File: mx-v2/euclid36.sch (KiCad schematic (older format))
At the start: 114 parts, among them SW1 RotaryEncoder_Switch, SW10 SW_PUSH, SW11 SW_PUSH, SW12 SW_PUSH, SW14 SW_PUSH, SW15 SW_PUSH, SW16 SW_PUSH, SW17 SW_PUSH, SW18 SW_PUSH, SW19 SW_PUSH, SW2 SW_PUSH, SW20 SW_PUSH, SW21 SW_PUSH, SW22 SW_PUSH, SW23 SW_PUSH, SW25 SW_PUSH, SW26 SW_PUSH, SW27 SW_PUSH, SW28 SW_PUSH, SW29 SW_PUSH, SW3 SW_PUSH, SW31 SW_PUSH, SW32 SW_PUSH, SW33 SW_PUSH, SW34 SW_PUSH, SW35 SW_PUSH, SW37 SW_PUSH, SW38 SW_PUSH, SW39 SW_PUSH, SW4 SW_PUSH, SW40 SW_PUSH, SW41 SW_PUSH, SW42 SW_PUSH, SW5 SW_PUSH, SW6 SW_PUSH, SW7 RotaryEncoder_Switch, SW8 SW_PUSH, SW9 SW_PUSH, U1 USBLC6-2SC6, U2 ATmega32U4-AU, Y1 XTAL

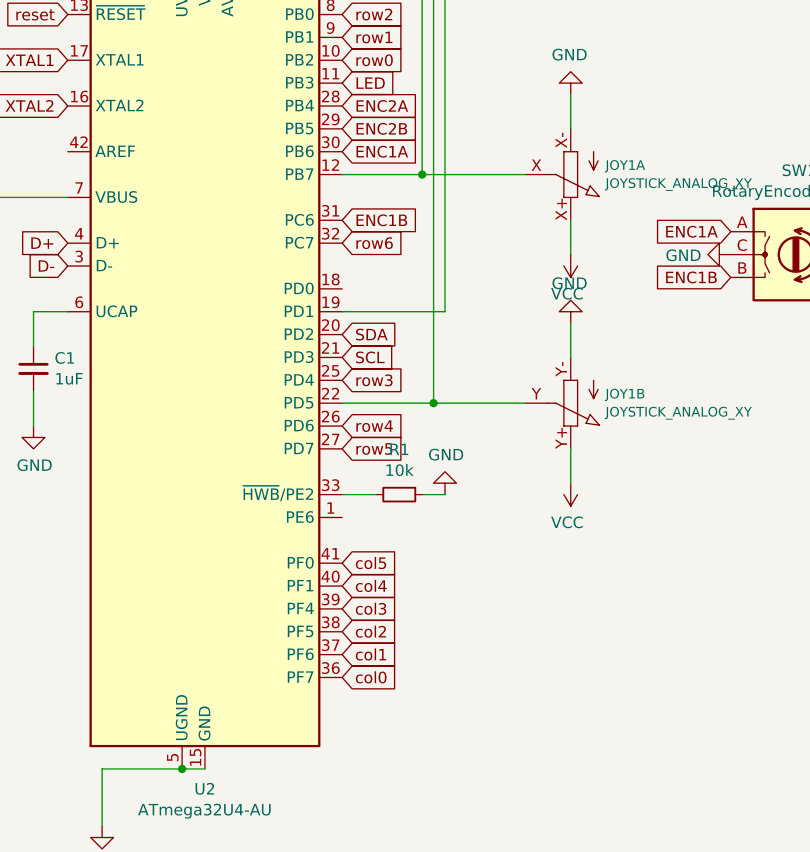
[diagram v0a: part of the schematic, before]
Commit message: accidentally wired my analog joysticks to digital inputs
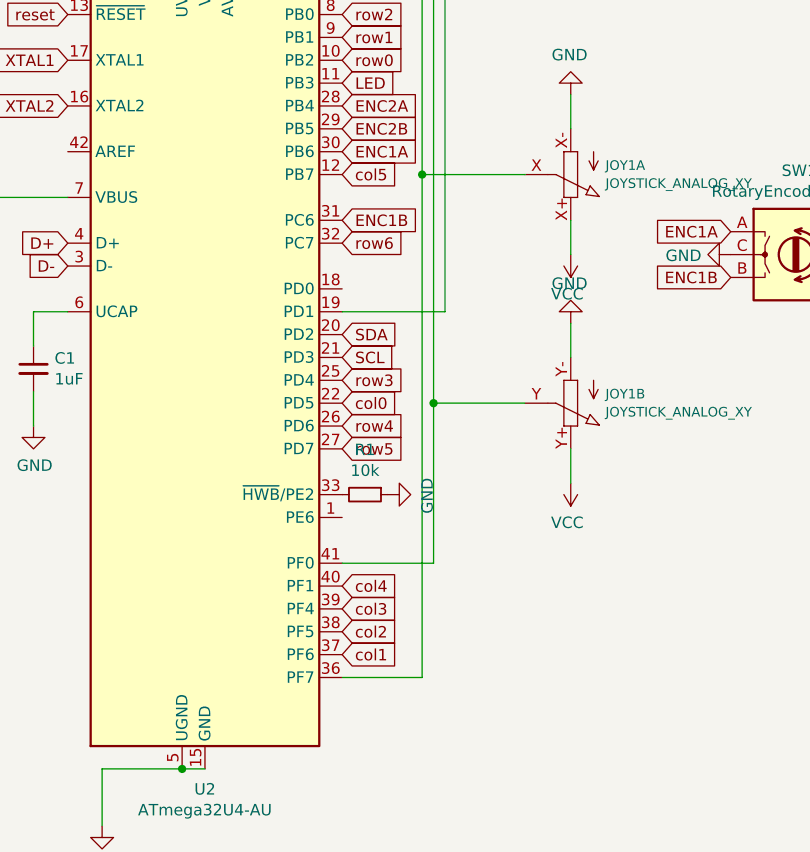
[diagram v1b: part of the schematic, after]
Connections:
- net col0: now also U2.22 (PD5); no longer U2.36 (PF7)
- net col5: now also U2.12 (PB7); no longer U2.41 (PF0)
- net at JOY1.X (S), S1.V2 (V): now also U2.36 (PF7); no longer U2.12 (PB7)
- net at JOY1.Y (S), S1.H2 (H): now also U2.41 (PF0); no longer U2.22 (PD5)
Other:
- moved on the sheet: R1
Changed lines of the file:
@@
 L Device:R_Small R1
 U 1 1 60688D69
-P 2550 3950
-F 0 "R1" V 2354 3950 50  0000 C CNN
-F 1 "10k" V 2445 3950 50  0000 C CNN
-F 2 "Resistor_SMD:R_0805_2012Metric" H 2550 3950 50  0001 C CNN
-F 3 "~" H 2550 3950 50  0001 C CNN
-F 4 "C17414" V 2550 3950 50  0001 C CNN "LCSC"
-	1    2550 3950
+P 2400 3950
+F 0 "R1" V 2204 3950 50  0000 C CNN
+F 1 "10k" V 2295 3950 50  0000 C CNN
+F 2 "Resistor_SMD:R_0805_2012Metric" H 2400 3950 50  0001 C CNN
+F 3 "~" H 2400 3950 50  0001 C CNN
+F 4 "C17414" V 2400 3950 50  0001 C CNN "LCSC"
+	1    2400 3950
 	0    1    1    0
 $EndComp
@@
 L power:GND #PWR0103
 U 1 1 6068E7A9
-P 2750 3950
-F 0 "#PWR0103" H 2750 3700 50  0001 C CNN
-F 1 "GND" H 2755 3777 50  0000 C CNN
-F 2 "" H 2750 3950 50  0001 C CNN
-F 3 "" H 2750 3950 50  0001 C CNN
-	1    2750 3950
-	1    0    0    1
-$EndComp
-Wire Wire Line
-	2450 3950 2300 3950
+P 2500 3950
+F 0 "#PWR0103" H 2500 3700 50  0001 C CNN
+F 1 "GND" H 2505 3777 50  0000 C CNN
+F 2 "" H 2500 3950 50  0001 C CNN
+F 3 "" H 2500 3950 50  0001 C CNN
+	1    2500 3950
+	0    -1   1    0
+$EndComp
 $Comp
 L Device:C_Small C1
@@
 Wire Wire Line
 	1750 7600 1750 7650
-Text GLabel 2300 4750 2    50   Input ~ 0
+Text GLabel 2300 3550 2    50   Input ~ 0
 col0
 Text GLabel 2300 4650 2    50   Input ~ 0
@@
 Text GLabel 2300 4350 2    50   Input ~ 0
 col4
-Text GLabel 2300 4250 2    50   Input ~ 0
+Text GLabel 2300 2550 2    50   Input ~ 0
 col5
 Text GLabel 2300 2050 2    50   Input ~ 0
@@
 Wire Wire Line
 	1800 1550 1700 1550
-Wire Wire Line
-	2650 3950 2750 3950
 $Comp
 L MCU_Microchip_ATmega:ATmega32U4-A U2
@@
 $EndComp
 Wire Wire Line
-	2300 2550 2650 2550
-Wire Wire Line
 	2650 2550 2650 850
 Wire Wire Line
 	2650 850  3300 850
-Wire Wire Line
-	2300 3550 2700 3550
 Wire Wire Line
 	2700 3550 2700 1250
@@
 Wire Wire Line
 	3100 3550 2700 3550
-Connection ~ 2700 3550
 Wire Wire Line
 	2750 1550 3300 1550
 Wire Wire Line
 	2650 2550 3100 2550
-Connection ~ 2650 2550
 $Comp
 L power:GND #PWR0122
@@
 	0    -1   -1   0
 $EndComp
+Wire Wire Line
+	2700 3550 2700 4250
+Wire Wire Line
+	2700 4250 2300 4250
+Connection ~ 2700 3550
+Wire Wire Line
+	2650 4750 2300 4750
+Connection ~ 2650 2550
+Wire Wire Line
+	2650 2550 2650 4750
 $EndSCHEMATC

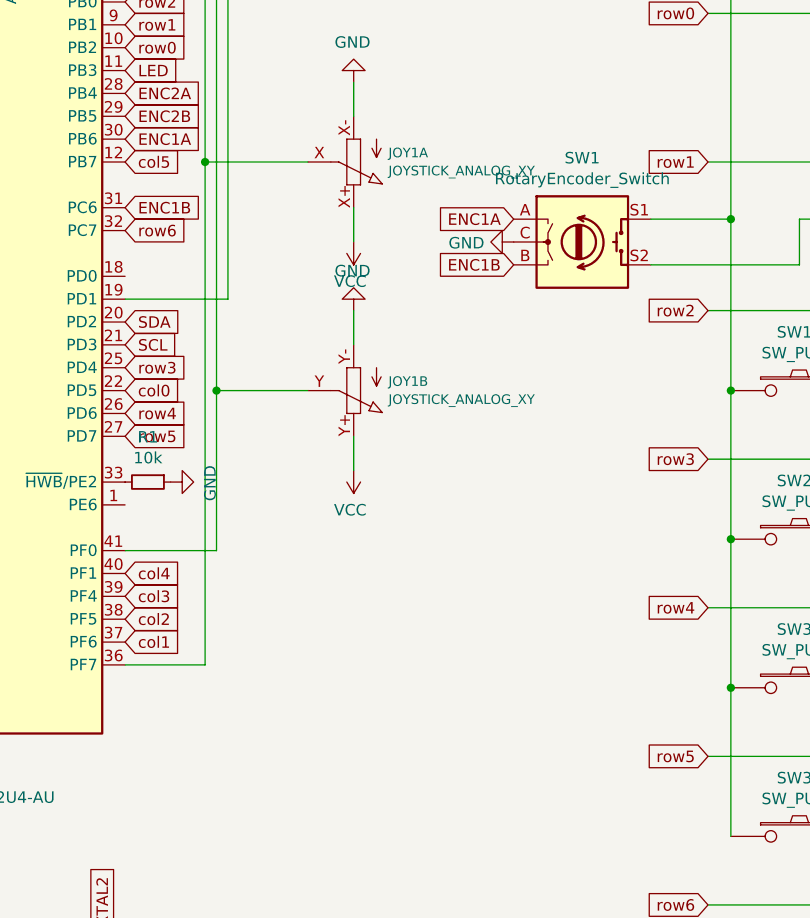
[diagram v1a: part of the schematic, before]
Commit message: added support for another joystick type, psp, as well as readme update with new feature layout image
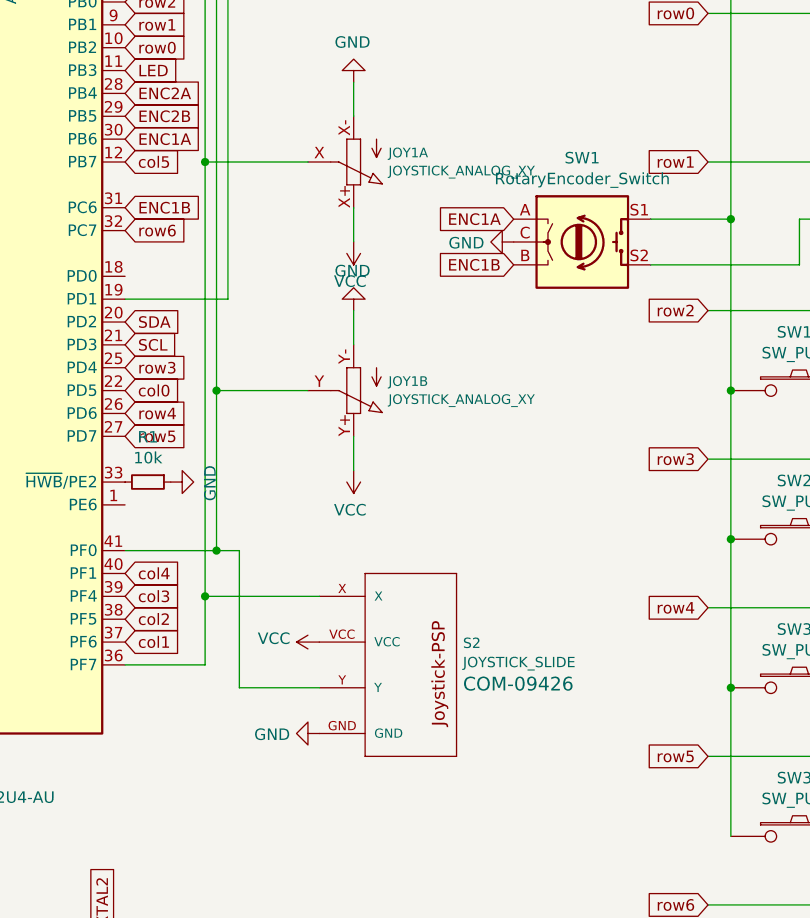
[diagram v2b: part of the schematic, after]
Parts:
- added S2: JOYSTICK_SLIDE, SparkFun-Switches:JOYSTICK-PSP1000, symbol SparkFun-Switches:JOYSTICK_SLIDE
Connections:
- net GND: now also S2.GND
- net VCC: now also S2.VCC
- net at JOY1.X (S), S1.V2 (V), U2.36 (PF7): now also S2.X
- net at JOY1.Y (S), S1.H2 (H), U2.41 (PF0): now also S2.Y
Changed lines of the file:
@@
 Connection ~ 2650 2550
 Wire Wire Line
-	2650 2550 2650 4750
+	2650 2550 2650 4450
+$Comp
+L SparkFun-Switches:JOYSTICK_SLIDE S2
+U 1 1 6093678C
+P 3550 4850
+F 0 "S2" H 3778 5045 45  0000 L CNN
+F 1 "JOYSTICK_SLIDE" H 3778 4961 45  0000 L CNN
+F 2 "SparkFun-Switches:JOYSTICK-PSP1000" H 3550 5500 20  0001 C CNN
+F 3 "" H 3550 4850 50  0001 C CNN
+F 4 "COM-09426" H 3778 4866 60  0000 L CNN "Field4"
+	1    3550 4850
+	1    0    0    -1
+$EndComp
+$Comp
+L power:VCC #PWR012
+U 1 1 60937C14
+P 3150 4650
+F 0 "#PWR012" H 3150 4500 50  0001 C CNN
+F 1 "VCC" V 3165 4777 50  0000 L CNN
+F 2 "" H 3150 4650 50  0001 C CNN
+F 3 "" H 3150 4650 50  0001 C CNN
+	1    3150 4650
+	0    -1   -1   0
+$EndComp
+$Comp
+L power:GND #PWR013
+U 1 1 60939355
+P 3150 5050
+F 0 "#PWR013" H 3150 4800 50  0001 C CNN
+F 1 "GND" V 3155 4922 50  0000 R CNN
+F 2 "" H 3150 5050 50  0001 C CNN
+F 3 "" H 3150 5050 50  0001 C CNN
+	1    3150 5050
+	0    1    1    0
+$EndComp
+Wire Wire Line
+	3150 4450 2650 4450
+Connection ~ 2650 4450
+Wire Wire Line
+	2650 4450 2650 4750
+Wire Wire Line
+	3150 4850 2800 4850
+Wire Wire Line
+	2800 4850 2800 4250
+Wire Wire Line
+	2800 4250 2700 4250
+Connection ~ 2700 4250
 $EndSCHEMATC

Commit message: Proto V2 complete and ordered from jlcpcb.com
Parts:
- C7, C8: LCSC C520058 -> C1804
- U1: LCSC C7519 -> C558442
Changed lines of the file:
@@
 F 2 "Capacitor_SMD:C_0805_2012Metric_Pad1.18x1.45mm_HandSolder" H 1200 6450 50  0001 C CNN
 F 3 "~" H 1200 6450 50  0001 C CNN
-F 4 "C520058" H 1200 6450 50  0001 C CNN "LCSC"
+F 4 "C1804" H 1200 6450 50  0001 C CNN "LCSC"
 	1    1200 6450
 	1    0    0    -1
@@
 F 2 "Capacitor_SMD:C_0805_2012Metric_Pad1.18x1.45mm_HandSolder" H 2200 6450 50  0001 C CNN
 F 3 "~" H 2200 6450 50  0001 C CNN
-F 4 "C520058" H 2200 6450 50  0001 C CNN "LCSC"
+F 4 "C1804" H 2200 6450 50  0001 C CNN "LCSC"
 	1    2200 6450
 	1    0    0    -1
@@
 F 2 "Package_TO_SOT_SMD:SOT-23-6" H 8800 8650 50  0001 C CNN
 F 3 "https://www.st.com/resource/en/datasheet/usblc6-2.pdf" H 9000 9500 50  0001 C CNN
-F 4 "C7519" H 8800 9150 50  0001 C CNN "LCSC"
+F 4 "C558442" H 8800 9150 50  0001 C CNN "LCSC"
 	1    8800 9150
 	0    1    1    0

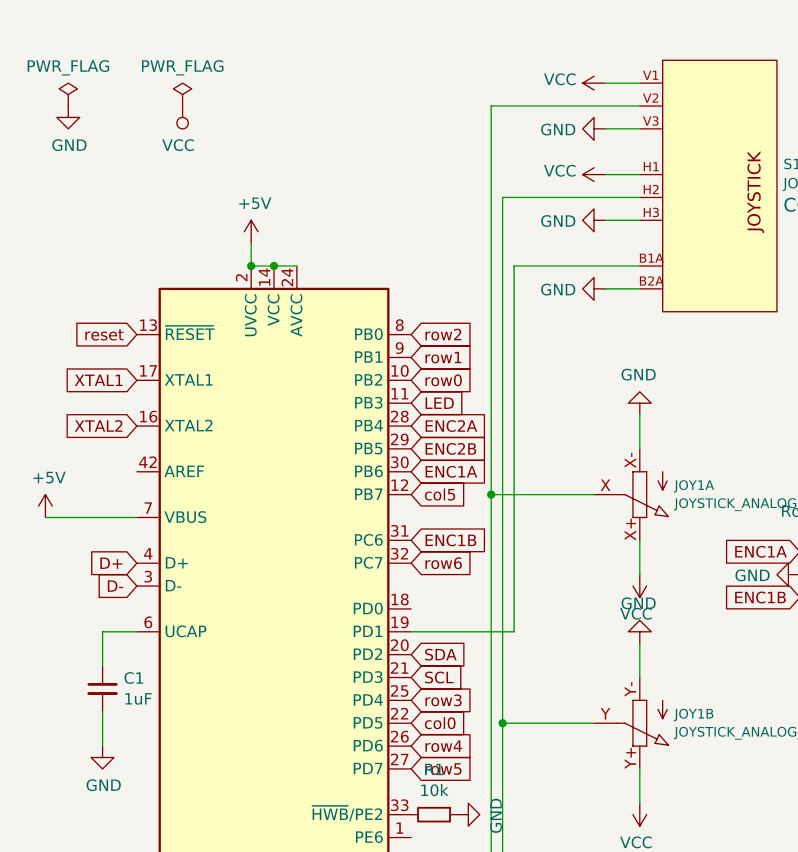
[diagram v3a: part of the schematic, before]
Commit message: last revision had a few problems, fixed some, see todo.txt
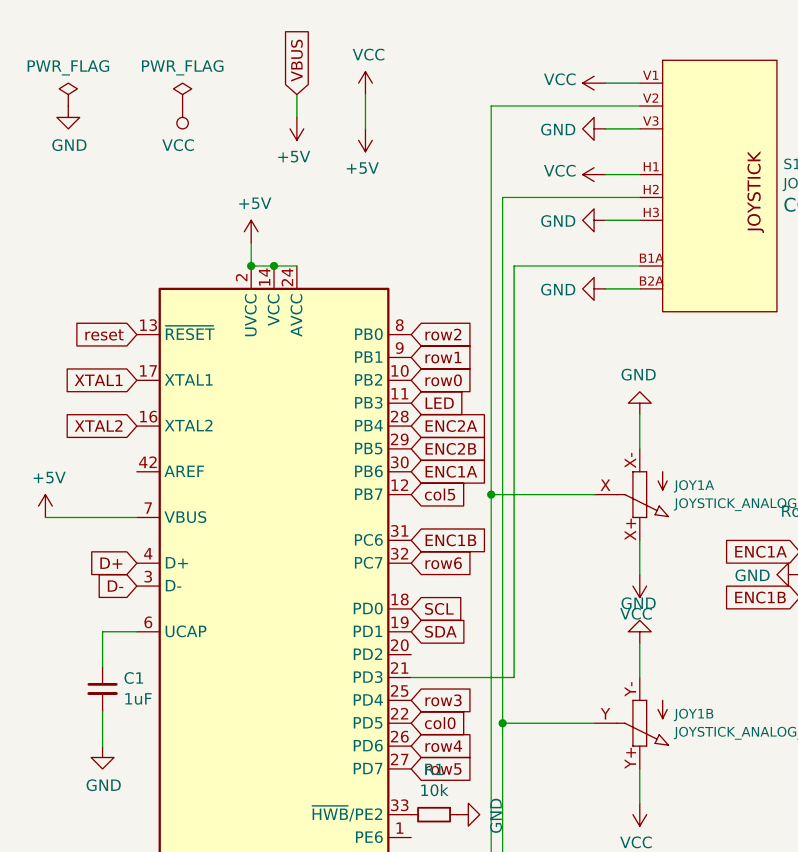
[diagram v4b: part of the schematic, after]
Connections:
- net VBUS is gone; now on net +5V: C9.1, R8.1, U1.5 (VBUS), USB1.11 (VBUS), USB1.2 (VBUS)
- net VCC is gone; now on net +5V: JOY1.X+ (E), JOY1.Y+ (E), L1.1 (VDD), L10.1 (VDD), L11.1 (VDD), L12.1 (VDD), L13.1 (VDD), L2.1 (VDD), L3.1 (VDD), L4.1 (VDD), L5.1 (VDD), L6.1 (VDD), L7.1 (VDD), L8.1 (VDD), L9.1 (VDD), OL1.3 (VCC), S1.H1 (H+), S1.V1 (V+), S2.VCC
- net SCL: now also U2.18 (PD0); no longer U2.21 (PD3)
- net SDA: now also U2.19 (PD1); no longer U2.20 (PD2)
- net at S1.B1A (SEL+): now also U2.21 (PD3); no longer U2.19 (PD1)
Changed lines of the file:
@@
 Wire Wire Line
 	1750 9300 1500 9300
-Text GLabel 2300 3250 2    50   Input ~ 0
+Text GLabel 2300 3150 2    50   Input ~ 0
 SDA
-Text GLabel 2300 3350 2    50   Input ~ 0
+Text GLabel 2300 3050 2    50   Input ~ 0
 SCL
 Text GLabel 4000 2800 0    50   Input ~ 0
@@
 	3150 1350 3300 1350
 Wire Wire Line
-	2750 1550 2750 3150
-Wire Wire Line
-	2750 3150 2300 3150
-Wire Wire Line
 	3100 3550 2700 3550
 Wire Wire Line
@@
 	2800 4250 2700 4250
 Connection ~ 2700 4250
+Text GLabel 1800 800  1    50   Input ~ 0
+VBUS
+$Comp
+L power:+5V #PWR?
+U 1 1 609F3BED
+P 1800 900
+F 0 "#PWR?" H 1800 750 50  0001 C CNN
+F 1 "+5V" H 1815 1073 50  0000 C CNN
+F 2 "" H 1800 900 50  0001 C CNN
+F 3 "" H 1800 900 50  0001 C CNN
+	1    1800 900
+	-1   0    0    1
+$EndComp
+Wire Wire Line
+	1800 800  1800 900
+Wire Wire Line
+	2750 3350 2300 3350
+Wire Wire Line
+	2750 1550 2750 3350
+$Comp
+L power:VCC #PWR?
+U 1 1 60CDE125
+P 2100 800
+F 0 "#PWR?" H 2100 650 50  0001 C CNN
+F 1 "VCC" H 2115 973 50  0000 C CNN
+F 2 "" H 2100 800 50  0001 C CNN
+F 3 "" H 2100 800 50  0001 C CNN
+	1    2100 800
+	1    0    0    -1
+$EndComp
+$Comp
+L power:+5V #PWR?
+U 1 1 60CDF6C3
+P 2100 950
+F 0 "#PWR?" H 2100 800 50  0001 C CNN
+F 1 "+5V" H 2115 1123 50  0000 C CNN
+F 2 "" H 2100 950 50  0001 C CNN
+F 3 "" H 2100 950 50  0001 C CNN
+	1    2100 950
+	-1   0    0    1
+$EndComp
+Wire Wire Line
+	2100 800  2100 950
 $EndSCHEMATC
